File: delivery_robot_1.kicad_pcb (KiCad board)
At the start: 4 copper layers, 100 x 100 mm, 159 parts, among them J1 SWD, J10 Port C/D breakout, J13 Pi 5 link, J14 Pi 5 power, J15 Motor2 encoder, J16 MDD20A PWM2/DIR2/GND, J17 Latch servo, J18 AUX1 Notecard, J19 AUX2 LiDAR, J2 XT30PW-M, J20 AUX3 GNSS, J21 AUX4 IMU, J22 AUX force-on, J4 BOOT0 jumper, J5 Power test points, J6 MDD20A PWM1/DIR1/GND, J7 Motor1 encoder, J8 Port A breakout, J9 Port B breakout, Q1 SQJ409EP, Q2 DMN63D8L, SW1 RESET, U1 STM32F091RCTx, U10 74LVC2G17, U2 TPSM63606RDLR, U3 TPS54202DDCR, U4 TPS7A8101DRBR, U5 TPSM63606RDLR, U6 USBLC6-4SC6, U7 USBLC6-4SC6, U8 SN74LVC1T45DBV, U9 74LVC2G17, Y3 8MHz

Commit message: Switch AUX ports to top-entry JST XH; drop encoder pull-ups and Pi sense
- J18-J21 (peripheral 5 V ports) are now top-entry JST XH B2B-XH-A:
  cables plug in from above, which suits a flat board you reach into,
  and the footprint drops from 107 to 58 mm2 per port. Use pre-made
  2-pin XH cables, so no crimping.
- Remove the DNP encoder pull-ups R48-R51. If the am-3651 outputs turn
  out to be open-collector, bodge 4.7k from each A/B line to ENCn_5V
  (noted on the Motor Control sheet).
- Remove the Pi-alive sense R44/R45. PA1 is a spare pin again (J8 pin
  2); the Pi's 3V3 on J13 still enables the AUX buck through D15.
- Board: same edits as Update PCB from Schematic (J18-J21 swapped,
  six resistors deleted, PA1 net restored on U1/J8); the parked parts
  are re-grouped beside the board. Venya's tracks unchanged (87).
- Docs, README and schematic PDF updated.

ERC 0/0. DRC: 0 errors, 3 existing text-size warnings, parity clean.
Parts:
- removed R44: 10k, Resistor_SMD:R_0805_2012Metric
- removed R45: 100k, Resistor_SMD:R_0805_2012Metric
- removed R48, R49, R50, R51: 4.7k, Resistor_SMD:R_0805_2012Metric
- J18, J19, J20, J21: footprint Connector_JST:JST_XH_S2B-XH-A_1x02_P2.50mm_Horizontal -> Connector_JST:JST_XH_B2B-XH-A_1x02_P2.50mm_Vertical
- moved C47 10.9 mm to (224.5, 118.2)
- moved C48 10.9 mm to (224.5, 129.2)
- moved F8 10.9 mm to (218.7, 118.6)
- moved F9 10.9 mm to (218.7, 129.6)
- moved R47 10.9 mm to (229.5, 86.4)
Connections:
- net PI_3V3_SENSE renamed PA1
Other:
- board text added: "AUX ports - J18-J21 top-entry XH, near an edge you can reach; PTC F4-F7 at each"
- board text added: "Pi link - AUX enable near U5, reset/BOOT0 near the MCU"
- board text removed: "AUX ports - J18-J21 on a board edge, PTC F4-F7 at each"
- board text removed: "Pi link - AUX enable near U5, reset/BOOT0/sense near the MCU"

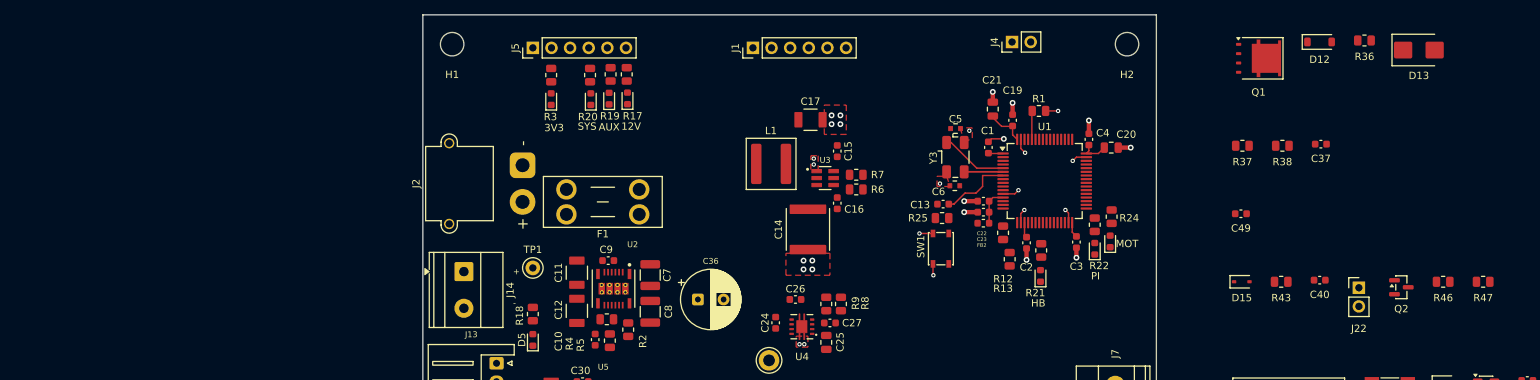
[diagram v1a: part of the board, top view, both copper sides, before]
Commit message: Place input protection and start AUX/servo placement
- Place the input protection parts beside J2/F1: Q1, D12, D13, R36.
- Place C37, C49 and R37/R38, and move C1 to fit.
- Park the AUX/servo parts (J22, Q2, D15, C40, R43, R46, R47) left of
  the board outline ready for placement.
- Rework +3V3/GND routing around the new parts (2 +3V3 segments
  removed, 3 GND tracks and 3 GND vias added).
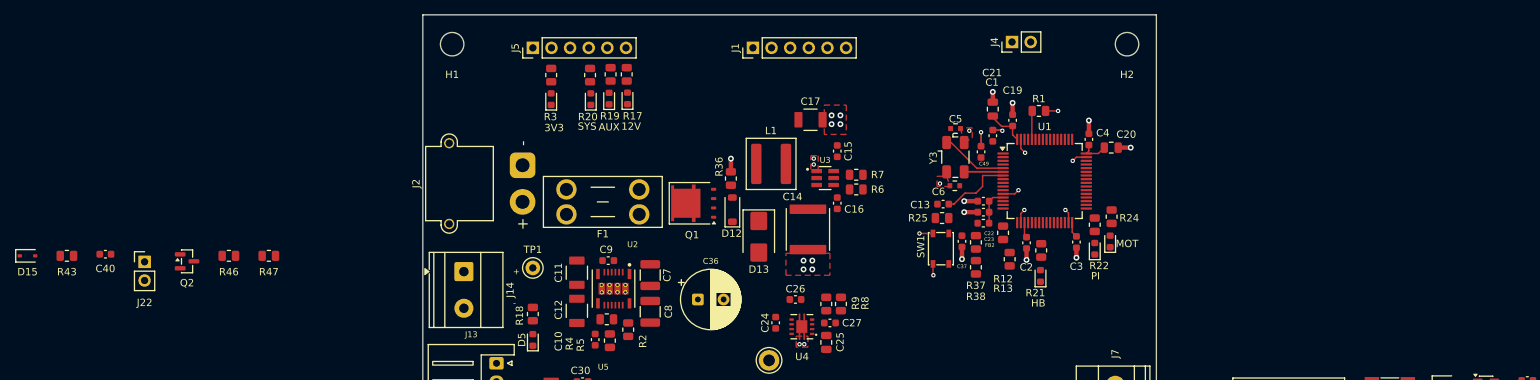
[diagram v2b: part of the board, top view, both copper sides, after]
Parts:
- moved Q2 165.6 mm to (52.9, 83.6)
- moved C40 165.6 mm to (41.7, 82.6)
- moved D15 165.6 mm to (31.1, 82.8)
- moved J22 165.6 mm to (47.1, 83.7)
- moved R46 165.6 mm to (58.6, 82.8)
- moved R43 165.6 mm to (36.5, 82.8)
- moved R47 165.6 mm to (64.0, 82.8)
- moved D13 93.5 mm to (130.8, 80.2), turned to -90 degrees
- moved R36 88.4 mm to (127.0, 72.3), turned to 90 degrees
- moved D12 83.2 mm to (127.2, 76.5), turned to 90 degrees
- moved Q1 79.5 mm to (121.9, 75.7), turned to 180 degrees
- moved C37 50.7 mm to (158.5, 80.9), turned to -90 degrees
- moved R38 44.9 mm to (160.4, 84.4), turned to -90 degrees
- moved R37 38.6 mm to (160.4, 81.0), turned to 90 degrees
- moved C49 36.4 mm to (161.1, 68.7), turned to 90 degrees
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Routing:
- net GND: track 30.7 -> 35.2 mm, vias 31 -> 34
- net +3V3: track 15.8 -> 13.8 mm
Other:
- board text removed: "Battery sense - divider near PA0"
- board text removed: "Input protection - after F1 (Q1 tab toward F1; D13 TVS next to C36)"
- board text removed: "U3 HF input cap - at U3 VIN (pin 3) / GND (pin 1)"

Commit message: Route the board and apply the prototype PCB checklist fixes
Routing
- Route power (pours, In2 power areas, vias) and all signals; add a
  Signal net class (0.15 mm width/clearance) for low-speed nets.
- J8 expansion header is now a 2x8 near the MCU.

Checklist red flags
- Crystal Y3 moved beside U1's OSC pins with C5/C6 outboard and no
  other signals under it.
- Vias untented by default (tented only under silkscreen); 15 mil
  test vias on key signals, recorded as DRC exclusions.
- ESD: U6/U7 split into four USBLC6-2SC6 (U6, U11, U7, U12), one per
  connector, with VBUS caps C50/C51; R12/R13 moved next to J13.
- GND test loop TP3 moved to the top edge beside J5.

Improvements
- Encoder connectors J7/J15 changed to keyed JST XH S4B side-entry.
- 43 passives/LEDs/FB2 moved from 0603 to 0805 (MPNs updated).
- Fifth M3 mounting hole H5 under J8.
- +3.3VA rerouted away from the crystal; acute track angles removed.
- Datasheet links filled in; silkscreen pin labels, pin maps, team
  names and date; reference labels cleared off pads and vias.
- Custom DRC rule for the J7/J15 silkscreen edge overhang.
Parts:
- removed J10: Port C/D breakout, Connector_PinHeader_2.54mm:PinHeader_1x18_P2.54mm_Vertical
- removed J9: Port B breakout, Connector_PinHeader_2.54mm:PinHeader_1x17_P2.54mm_Vertical
- added C50: 100nF, Capacitor_SMD:C_0805_2012Metric, F.Cu at (162.0, 138.8)
- added C51: 100nF, Capacitor_SMD:C_0805_2012Metric, F.Cu at (171.5, 120.2)
- added H5: M3, MountingHole:MountingHole_3.2mm_M3, F.Cu at (132.0, 124.5)
- added U11: USBLC6-2SC6, Package_TO_SOT_SMD:SOT-23-6, F.Cu at (162.0, 142.5)
- added U12: USBLC6-2SC6, Package_TO_SOT_SMD:SOT-23-6, F.Cu at (171.6, 123.4)
- C1, C10, C13, C15, C16, C19, C2, C22, C23, C24, C26, C27, C3, C30, C31, C34, C35, C37, C38, C39, C4, C40, C41, C42, C43, C44, C45, C46, C47, C48, C49, C9: footprint Capacitor_SMD:C_0603_1608Metric -> Capacitor_SMD:C_0805_2012Metric
- C5, C6: footprint project_footprints:C_Murata_GRM1885C1H160JA01 -> Capacitor_SMD:C_0805_2012Metric
- D11, D3, D4, D5, D6, D7, D8, D9: footprint LED_SMD:LED_0603_1608Metric -> LED_SMD:LED_0805_2012Metric
- FB2: footprint Inductor_SMD:L_0603_1608Metric -> Inductor_SMD:L_0805_2012Metric
- J15, J7: footprint TerminalBlock_Phoenix:TerminalBlock_Phoenix_MKDS-1,5-4_1x04_P5.00mm_Horizontal -> Connector_JST:JST_XH_S4B-XH-A_1x04_P2.50mm_Horizontal
- J8: value Port A breakout -> Expansion header; footprint Connector_PinHeader_2.54mm:PinHeader_1x15_P2.54mm_Vertical -> Connector_PinHeader_2.54mm:PinHeader_2x08_P2.54mm_Vertical
- U6, U7: value USBLC6-4SC6 -> USBLC6-2SC6
- moved R42 147.2 mm to (119.8, 62.8), turned to 90 degrees
- moved F7 133.2 mm to (130.9, 144.9)
- moved F6 125.7 mm to (119.9, 144.9)
- moved J21 120.4 mm to (133.0, 151.0)
- moved F5 118.3 mm to (108.9, 144.9)
- moved D14 113.6 mm to (117.2, 62.1)
- moved J20 113.0 mm to (122.0, 151.0)
- moved F4 110.8 mm to (97.9, 144.9)
- moved J19 105.5 mm to (111.0, 151.0)
- moved Q2 103.8 mm to (156.6, 86.9), turned to 90 degrees
- moved R47 99.7 mm to (159.4, 53.8)
- moved F3 98.9 mm to (125.5, 63.0), turned to 180 degrees
- moved R46 98.2 mm to (156.5, 90.0)
- moved J18 98.0 mm to (100.0, 151.0)
- moved J17 85.6 mm to (128.1, 55.4), turned to 180 degrees
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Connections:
- J8 pad 1: VBAT_SENSE -> +3V3
- J8 pad 10: ENC2_B -> PC7
- J8 pad 11: PA10 -> PC10
- J8 pad 12: PA11 -> PC11
- J8 pad 13: PA12 -> PB6
- J8 pad 14: ENC1_A -> PB7
- J8 pad 15: GND -> PB9
- J8 pad 2: PA1 -> GND
- J8 pad 3: USART2_TX -> PC0
- J8 pad 4: USART2_RX -> PA1
- J8 pad 6: LED_USER -> PC2
- J8 pad 7: MOTOR1_PWM -> PB13
- J8 pad 8: MOTOR2_PWM -> PB15
- J8 pad 9: ENC2_A -> PC6
- U1 pad 11: PC3 -> unconnected-(U1-PC3-Pad11)
- U1 pad 2: USER_BTN -> unconnected-(U1-PC13-Pad2)
- U1 pad 24: PC4 -> unconnected-(U1-PC4-Pad24)
- U1 pad 25: PC5 -> unconnected-(U1-PC5-Pad25)
- U1 pad 27: PB1 -> unconnected-(U1-PB1-Pad27)
- U1 pad 3: OSC32_IN -> unconnected-(U1-PC14-Pad3)
- U1 pad 39: PC8 -> unconnected-(U1-PC8-Pad39)
- U1 pad 4: OSC32_OUT -> unconnected-(U1-PC15-Pad4)
- U1 pad 40: PC9 -> unconnected-(U1-PC9-Pad40)
- U1 pad 43: PA10 -> unconnected-(U1-PA10-Pad43)
- U1 pad 44: PA11 -> unconnected-(U1-PA11-Pad44)
- U1 pad 45: PA12 -> unconnected-(U1-PA12-Pad45)
- U1 pad 53: PC12 -> unconnected-(U1-PC12-Pad53)
- U1 pad 54: PD2 -> unconnected-(U1-PD2-Pad54)
- U1 pad 56: PB4 -> unconnected-(U1-PB4-Pad56)
- U1 pad 57: PB5 -> unconnected-(U1-PB5-Pad57)
- U1 pad 61: PB8 -> unconnected-(U1-PB8-Pad61)
- U1 pad 9: PC1 -> unconnected-(U1-PC1-Pad9)
- U6 pad 4: /Motor Control/MOTOR2_PWM_CONN -> /Motor Control/MOTOR1_DIR_CONN
- U6 pad 6: /Motor Control/MOTOR2_DIR_CONN -> /Motor Control/MOTOR1_PWM_CONN
- U7 pad 4: /Motor Control/ENC2_A_CONN -> /Motor Control/ENC1_B_CONN
- U7 pad 6: /Motor Control/ENC2_B_CONN -> /Motor Control/ENC1_A_CONN
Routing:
- net +3V3: track 13.8 -> 248.5 mm, vias 0 -> 25
- net +5V_SYS: track 0.00 -> 115.1 mm, vias 0 -> 16
- net MOTOR2_DIR: track 0.00 -> 95.9 mm, vias 0 -> 4
- net MOTOR2_PWM: track 0.00 -> 95.6 mm, vias 0 -> 5
- net /Pi 5 Interface/PI_BOOT0: track 0.00 -> 93.1 mm, vias 0 -> 5
- net MOTOR1_DIR: track 0.00 -> 92.5 mm, vias 0 -> 3
- net PB6: track 0.00 -> 86.1 mm, vias 0 -> 4
- net PB7: track 0.00 -> 79.5 mm, vias 0 -> 8
- net USART2_RX: track 0.00 -> 79.1 mm, vias 0 -> 4
- net USART2_TX: track 0.00 -> 77.5 mm, vias 0 -> 4
- net MOTOR1_PWM: track 0.00 -> 77.4 mm, vias 0 -> 7
- net +5V_AUX: track 0.00 -> 72.8 mm, vias 0 -> 19
- net PC0: track 0.00 -> 72.8 mm, vias 0 -> 2
- net /Servo Interface/SERVO_BUS: track 0.00 -> 72.8 mm, vias 0 -> 7
- net PA4: track 0.00 -> 70.8 mm, vias 0 -> 2
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- added copper zone on F.Cu, net +12V
- added copper zone on In2.Cu, net +12V
- added copper zone on In2.Cu, net +3V3
- added copper zone on F.Cu, net +5V_AUX
- added copper zone on In2.Cu, net +5V_AUX
- added copper zone on F.Cu, net +5V_PI
- added copper zone on F.Cu, net +5V_SYS
- added copper zone on In2.Cu, net +5V_SYS
- added copper zone on B.Cu, net /Servo Interface/VBAT_SERVO
- added copper zone on F.Cu, net /Servo Interface/VBAT_SERVO
- added copper zone on F.Cu, net VBAT_FUSED
- added copper zone on B.Cu, net VBAT_IN
- added copper zone on F.Cu, net VBAT_IN
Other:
- board size 100 x 100 mm -> 100 x 106 mm
- board text added: "1 3V3 2 EN"
- board text added: "1 5V 2 GND 3 A 4 B"
- board text added: "2026-10-20"
- board text added: "AUX J18-21: 1=5V 2=GND"
- board text added: "BT0"
- board text added: "CLK"
- board text added: "DIO"
- board text added: "DIR"
- board text added: "GND"
- board text added: "J5: 12V GND AUX SYS 3V3 3VA"
- board text added: "J8 even 2-16: GND PA1 PC2 PB15 PC7 PC11 PB7 GND"
- board text added: "J8 odd 1-15: 3V3 PC0 PA4 PB13 PC6 PC10 PB6 PB9"
- board text added: "PI5V"
- board text added: "PWM"
- board text added: "RST"
- board text added: "SIG"
- board text added: "V.Bhardwaj J.Yasuumi S.Chen M.Gagvani"
- board text added: "VB"
- board text removed: "AUX ports - J18-J21 top-entry XH, near an edge you can reach; PTC F4-F7 at each"
- board text removed: "Encoder 1 - buffer + RC between R28/R29 and the MCU, PTC/cap at J7"
- board text removed: "Encoder 2 - buffer + RC between R32/R33 and the MCU, PTC/cap at J15"
- board text removed: "Latch servo - J17 on a board edge, F3 + D14 at J17, U8 group near PB10/PB11"
- board text removed: "Motor driver - R52/R53 PWM pull-downs, F10/F11 in J6/J16 pin-3 ground"
- board text removed: "Pi link - AUX enable near U5, reset/BOOT0 near the MCU"

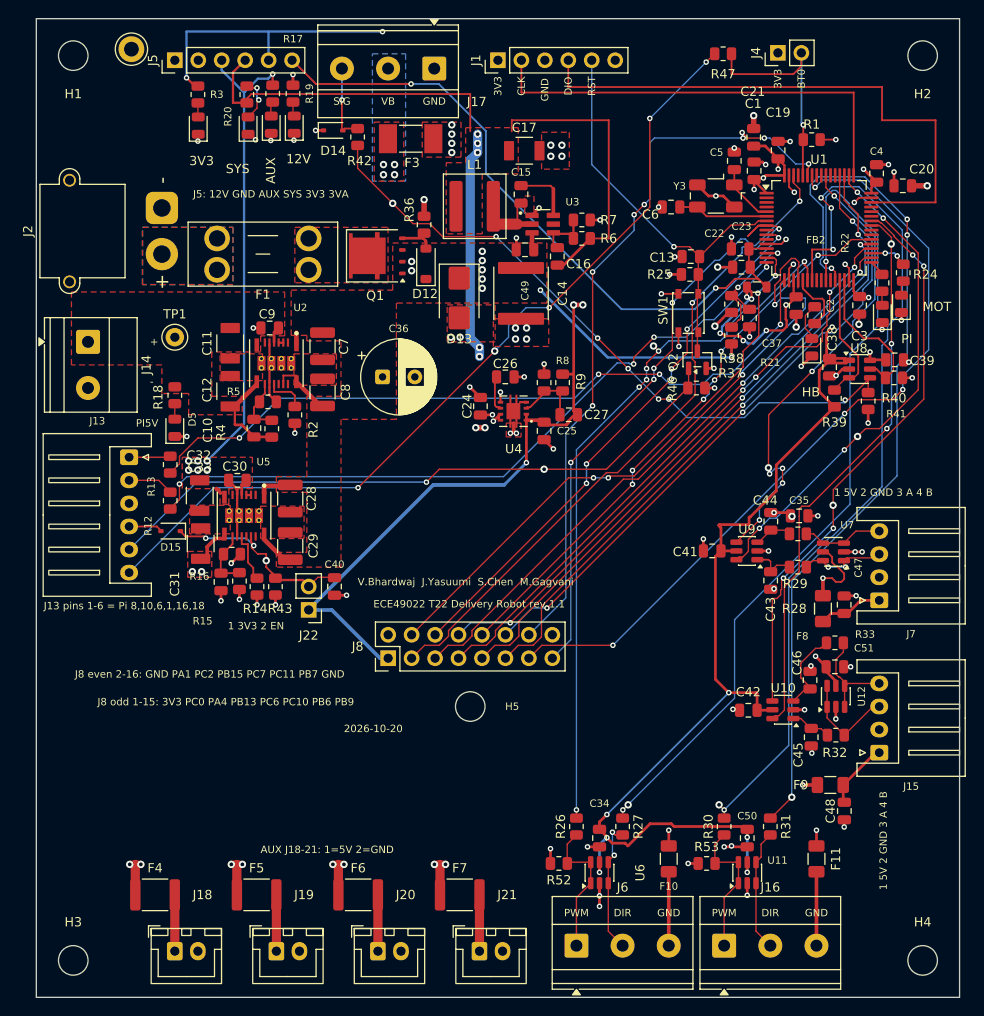
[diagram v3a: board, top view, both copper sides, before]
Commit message: Add outer-layer GND pours and stitching vias
- Board-wide GND pours on F.Cu and B.Cu at lowest priority (0.5 mm
  clearance, solid SMD / thermal THT connections, island removal).
- H5 copper keepout matching H1-H4; drop three redundant small F.Cu
  GND pours now covered by the full pour.
- GND straps on J8 pin 16 and J5 pin 2 to fix starved thermals.
- 165 GND stitching vias (6 mm grid, 5 mm edge row), kept clear of
  part bodies and silkscreen.
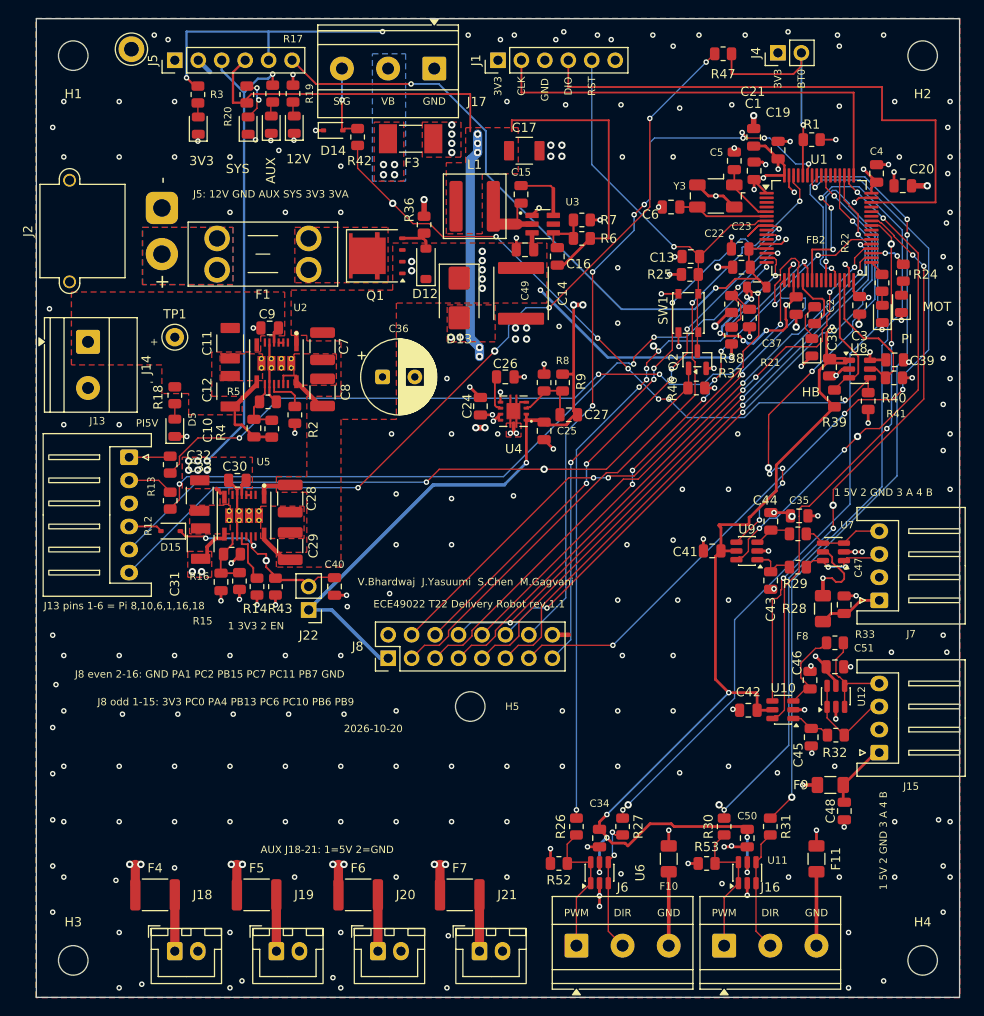
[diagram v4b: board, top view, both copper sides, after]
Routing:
- net GND: track 99.2 -> 102.8 mm, vias 88 -> 252
- added copper zone on B.Cu, net GND
